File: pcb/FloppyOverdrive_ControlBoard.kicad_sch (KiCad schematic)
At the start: 43 parts, among them J1 174804-1, J2 Motor_Header, J3 Bus_Connector, J4 Sensor_Header, J5 Heads_Header, J6 Step_Header, J7 PIC_ADC_Header, J8 FPGA_IO_Header, J9 HeadOut_Header, SW1 RST_Btn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

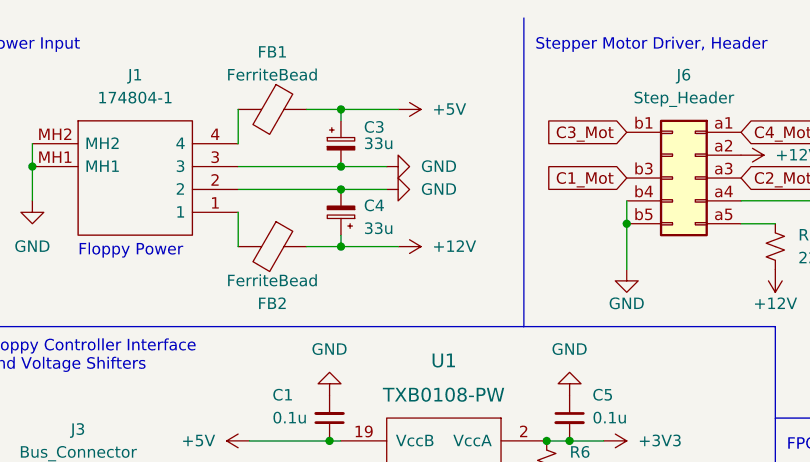
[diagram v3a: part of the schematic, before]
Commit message: Worked on PCB layout, began adding test points
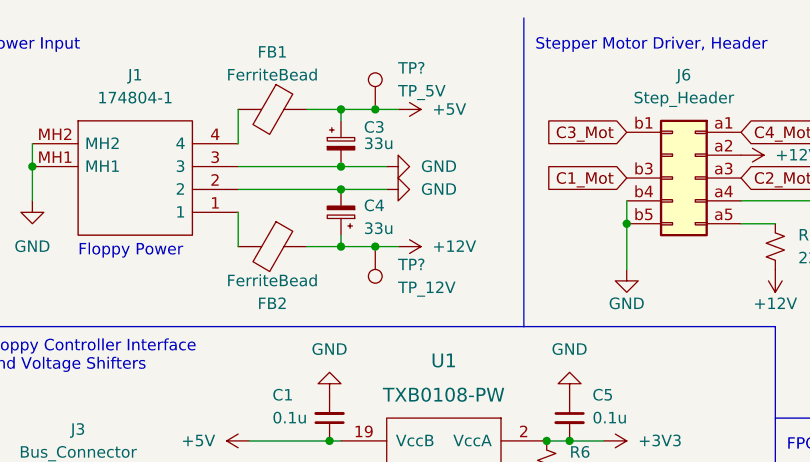
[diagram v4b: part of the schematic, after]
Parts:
- added TP?: TP_5V, symbol Connector:TestPoint
- added TP?: TP_12V, symbol Connector:TestPoint
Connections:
- net +12V: now also TP?.1
- net +5V: now also TP?.1
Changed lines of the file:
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@@
   (junction (at 76.2 185.42) (diameter 0) (color 0 0 0 0)
   )
+  (junction (at 55.88 21.59) (diameter 0) (color 0 0 0 0)
+  )
   (junction (at 77.47 105.41) (diameter 0) (color 0 0 0 0)
   )
@@
   (junction (at 16.51 101.6) (diameter 0) (color 0 0 0 0)
   )
+  (junction (at 55.88 36.83) (diameter 0) (color 0 0 0 0)
+  )
   (junction (at 16.51 83.82) (diameter 0) (color 0 0 0 0)
   )
@@
     (stroke (width 0) (type default) (color 0 0 0 0))
   )
-  (wire (pts (xy 52.07 36.83) (xy 58.42 36.83))
+  (wire (pts (xy 52.07 36.83) (xy 55.88 36.83))
     (stroke (width 0) (type default) (color 0 0 0 0))
   )
@@
     (stroke (width 0) (type default) (color 0 0 0 0))
   )
+  (wire (pts (xy 55.88 21.59) (xy 58.42 21.59))
+    (stroke (width 0) (type default) (color 0 0 0 0))
+  )
   (wire (pts (xy 74.93 71.12) (xy 76.2 71.12))
     (stroke (width 0) (type default) (color 0 0 0 0))
@@
     (stroke (width 0) (type default) (color 0 0 0 0))
   )
+  (wire (pts (xy 55.88 36.83) (xy 58.42 36.83))
+    (stroke (width 0) (type default) (color 0 0 0 0))
+  )
   (wire (pts (xy 24.13 158.75) (xy 26.67 158.75))
     (stroke (width 0) (type default) (color 0 0 0 0))
@@
     (stroke (width 0) (type default) (color 0 0 0 0))
   )
-  (wire (pts (xy 52.07 21.59) (xy 58.42 21.59))
+  (wire (pts (xy 52.07 21.59) (xy 55.88 21.59))
     (stroke (width 0) (type default) (color 0 0 0 0))
   )
@@
     (pin "2")
   )
+  (symbol (lib_id "Connector:TestPoint") (at 55.88 21.59 0) (unit 1)
+    (in_bom yes) (on_board yes) (fields_autoplaced)
+    (property "Reference" "TP?" (id 0) (at 58.42 17.0179 0)
+      (effects (font (size 1.27 1.27)) (justify left))
+    )
+    (property "Value" "TP_5V" (id 1) (at 58.42 19.5579 0)
+      (effects (font (size 1.27 1.27)) (justify left))
+    )
+    (property "Footprint" "" (id 2) (at 60.96 21.59 0)
+      (effects (font (size 1.27 1.27)) hide)
+    )
+    (property "Datasheet" "~" (id 3) (at 60.96 21.59 0)
+      (effects (font (size 1.27 1.27)) hide)
+    )
+    (pin "1")
+  )
   (symbol (lib_id "power:GND") (at 119.38 140.97 270) (unit 1)
     (in_bom yes) (on_board yes) (fields_autoplaced)
@@
     (pin "2")
   )
+  (symbol (lib_id "Connector:TestPoint") (at 55.88 36.83 180) (unit 1)
+    (in_bom yes) (on_board yes) (fields_autoplaced)
+    (property "Reference" "TP?" (id 0) (at 58.42 38.8619 0)
+      (effects (font (size 1.27 1.27)) (justify right))
+    )
+    (property "Value" "TP_12V" (id 1) (at 58.42 41.4019 0)
+      (effects (font (size 1.27 1.27)) (justify right))
+    )
+    (property "Footprint" "" (id 2) (at 50.8 36.83 0)
+      (effects (font (size 1.27 1.27)) hide)
+    )
+    (property "Datasheet" "~" (id 3) (at 50.8 36.83 0)
+      (effects (font (size 1.27 1.27)) hide)
+    )
+    (pin "1")
+  )
   (symbol (lib_id "Connector_Generic:Conn_02x02_Odd_Even") (at 124.46 80.01 0) (unit 1)
     (in_bom yes) (on_board yes) (fields_autoplaced)
@@
       (reference "SW1") (unit 1) (value "RST_Btn") (footprint "Button_Switch_THT:SW_PUSH_6mm")
     )
+    (path "/58a9337f-8e58-4970-873c-354ef45ae12f"
+      (reference "TP?") (unit 1) (value "TP_5V") (footprint "")
+    )
+    (path "/6c7d9ade-e7a5-41ce-947f-92e1c557904b"
+      (reference "TP?") (unit 1) (value "TP_12V") (footprint "")
+    )
     (path "/af8acdcd-2401-4236-bdc2-c260c5079e4e"

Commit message: Routing first draft
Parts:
- added TP3: TP_3V3, TestPoint:TestPoint_Pad_D1.0mm, symbol Connector:TestPoint
- TP1, TP2: renamed from TP?; footprint (none) -> TestPoint:TestPoint_Pad_D1.0mm
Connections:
- net +3.3V: no longer R11.2, U4.J2.34 (3v3)
- net +3V3: now also R11.2, U4.J2.34 (3v3), TP3.1
- net Density: now also U4.J3.20 (F14); no longer U4.J3.1 (A7)
- net DriveSel_0: now also U4.J3.26 (K14); no longer U4.J3.4 (C6)
- net DriveSel_1: now also U4.J3.28 (L14); no longer U4.J3.5 (D6)
- net DriveSel_2: now also U4.J3.30 (L12); no longer U4.J3.6 (D7)
- net DriveSel_3: now also U4.J3.22 (G14); no longer U4.J3.2 (A6)
- net Index: now also U4.J3.24 (H12); no longer U4.J3.3 (C7)
- net Motor: now also U4.J3.32 (P14); no longer U4.J3.7 (A10)
- net Motor_Control: now also U4.J2.29 (M6); no longer U4.J2.7 (C3)
- net PIN_10: now also U4.J3.5 (D6); no longer U4.J3.20 (F14)
- net PIN_12: now also U4.J3.6 (D7); no longer U4.J3.21 (F12)
- net PIN_14: now also U4.J3.7 (A10); no longer U4.J3.22 (G14)
- net PIN_16: now also U4.J3.8 (D10); no longer U4.J3.23 (G12)
- net PIN_18: now also U4.J3.9 (C10); no longer U4.J3.24 (H12)
- net PIN_2: now also U4.J3.1 (A7); no longer U4.J2.31 (M7)
- net PIN_20: now also U4.J3.10 (C11); no longer U4.J3.25 (J12)
- net PIN_22: now also U4.J3.11 (A11); no longer U4.J3.26 (K14)
- net PIN_24: now also U4.J3.12 (A12); no longer U4.J3.27 (H11)
- net PIN_26: now also U4.J3.13 (B14); no longer U4.J3.28 (L14)
- net PIN_28: now also U4.J3.14 (C14); no longer U4.J3.29 (K12)
- net PIN_30: now also U4.J3.15 (C12); no longer U4.J3.30 (L12)
- net PIN_32: now also U4.J3.16 (D14); no longer U4.J3.31 (N14)
- net PIN_34: now also U4.J3.17 (D12); no longer U4.J3.32 (P14)
- net PIN_36: now also U4.J3.18 (E14); no longer U4.J3.33 (M12)
- net PIN_38: now also U4.J2.27 (P3); no longer U4.J3.34 (P8)
- net PIN_4: now also U4.J3.2 (A6); no longer U4.J3.17 (D12)
- net PIN_6: now also U4.J3.3 (C7); no longer U4.J3.18 (E14)
- net PIN_8: now also U4.J3.4 (C6); no longer U4.J3.19 (E12)
- net ReadData: now also U4.J3.23 (G12); no longer U4.J3.14 (C14)
- net Ready: now also U4.J3.19 (E12); no longer U4.J3.16 (D14)
- net SideSel: now also U4.J3.21 (F12); no longer U4.J3.15 (C12)
- net Speed_Control: now also U4.J2.31 (M7); no longer U4.J2.9 (C1)
- net Step: now also U4.J3.33 (M12); no longer U4.J3.9 (C10)
- net StepDir: now also U4.J3.34 (P8); no longer U4.J3.8 (D10)
- net Track0: now also U4.J3.27 (H11); no longer U4.J3.12 (A12)
- net WriteData: now also U4.J3.31 (N14); no longer U4.J3.10 (C11)
- net WriteGate: now also U4.J3.29 (K12); no longer U4.J3.11 (A11)
- net WriteProtect: now also U4.J3.25 (J12); no longer U4.J3.13 (B14)
- net at U4.J2.11 (E1): now also J8.7 (Pin_7); no longer J8.3 (Pin_3)
- net at U4.J2.12 (D1): now also J8.9 (Pin_9); no longer J8.5 (Pin_5)
- net at U4.J2.13 (G1): now also J8.11 (Pin_11); no longer J8.7 (Pin_7)
- net at U4.J2.14 (F3): now also J8.13 (Pin_13); no longer J8.9 (Pin_9)
- net at U4.J2.15 (H1): now also J8.15 (Pin_15); no longer J8.11 (Pin_11)
- net at U4.J2.16 (G3): now also J8.17 (Pin_17); no longer J8.13 (Pin_13)
- net at U4.J2.17 (J1): now also J8.19 (Pin_19); no longer J8.15 (Pin_15)
- net at U4.J2.18 (H3): now also J8.21 (Pin_21); no longer J8.17 (Pin_17)
- net at U4.J2.19 (K3): now also J8.23 (Pin_23); no longer J8.19 (Pin_19)
- net at U4.J2.20 (J3): now also J8.25 (Pin_25); no longer J8.21 (Pin_21)
- net at U4.J2.21 (M1): now also J8.27 (Pin_27); no longer J8.23 (Pin_23)
- net at U4.J2.22 (L1): now also J8.29 (Pin_29); no longer J8.25 (Pin_25)
- net at U4.J2.23 (M3): now also J8.31 (Pin_31); no longer J8.27 (Pin_27)
- net at U4.J2.24 (N1): now also J8.33 (Pin_33); no longer J8.29 (Pin_29)
- net at U4.J2.25 (P2): now also J8.35 (Pin_35); no longer J8.31 (Pin_31)
- net at U4.J2.26 (P1): now also J8.37 (Pin_37); no longer J8.33 (Pin_33)
- new net: J8.3 (Pin_3), U4.J2.7 (C3)
- new net: J8.5 (Pin_5), U4.J2.9 (C1)
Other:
- moved on the sheet: J7, J8, R11, SW1

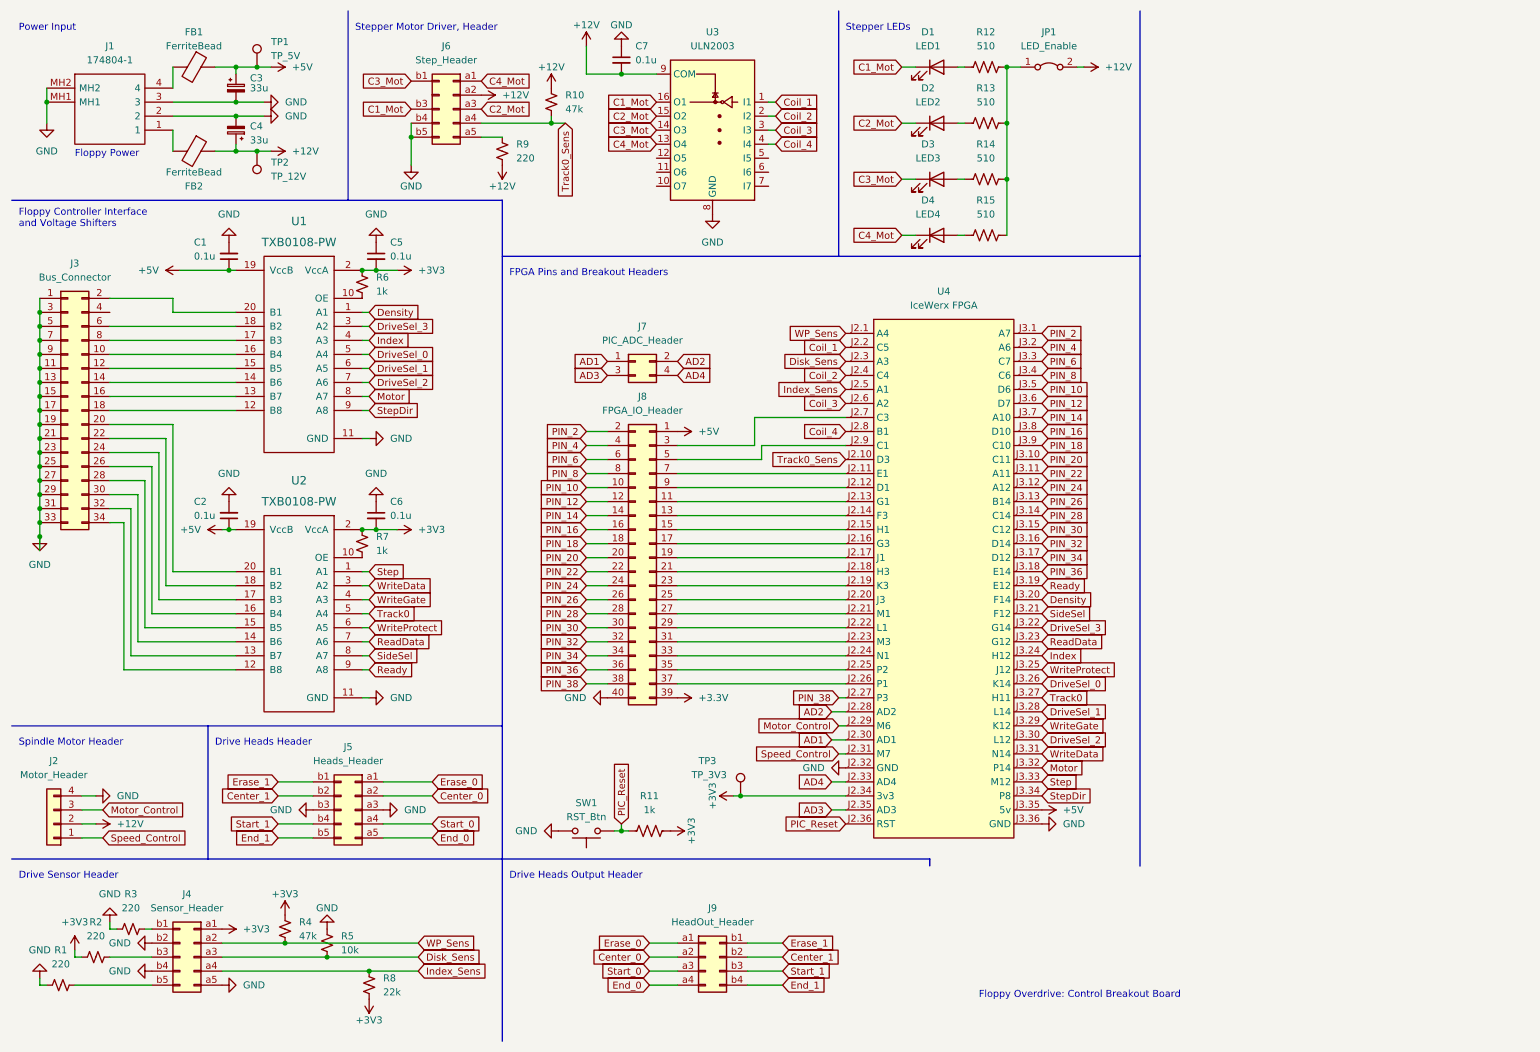
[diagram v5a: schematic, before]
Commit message: Fixed floppy bus orientation
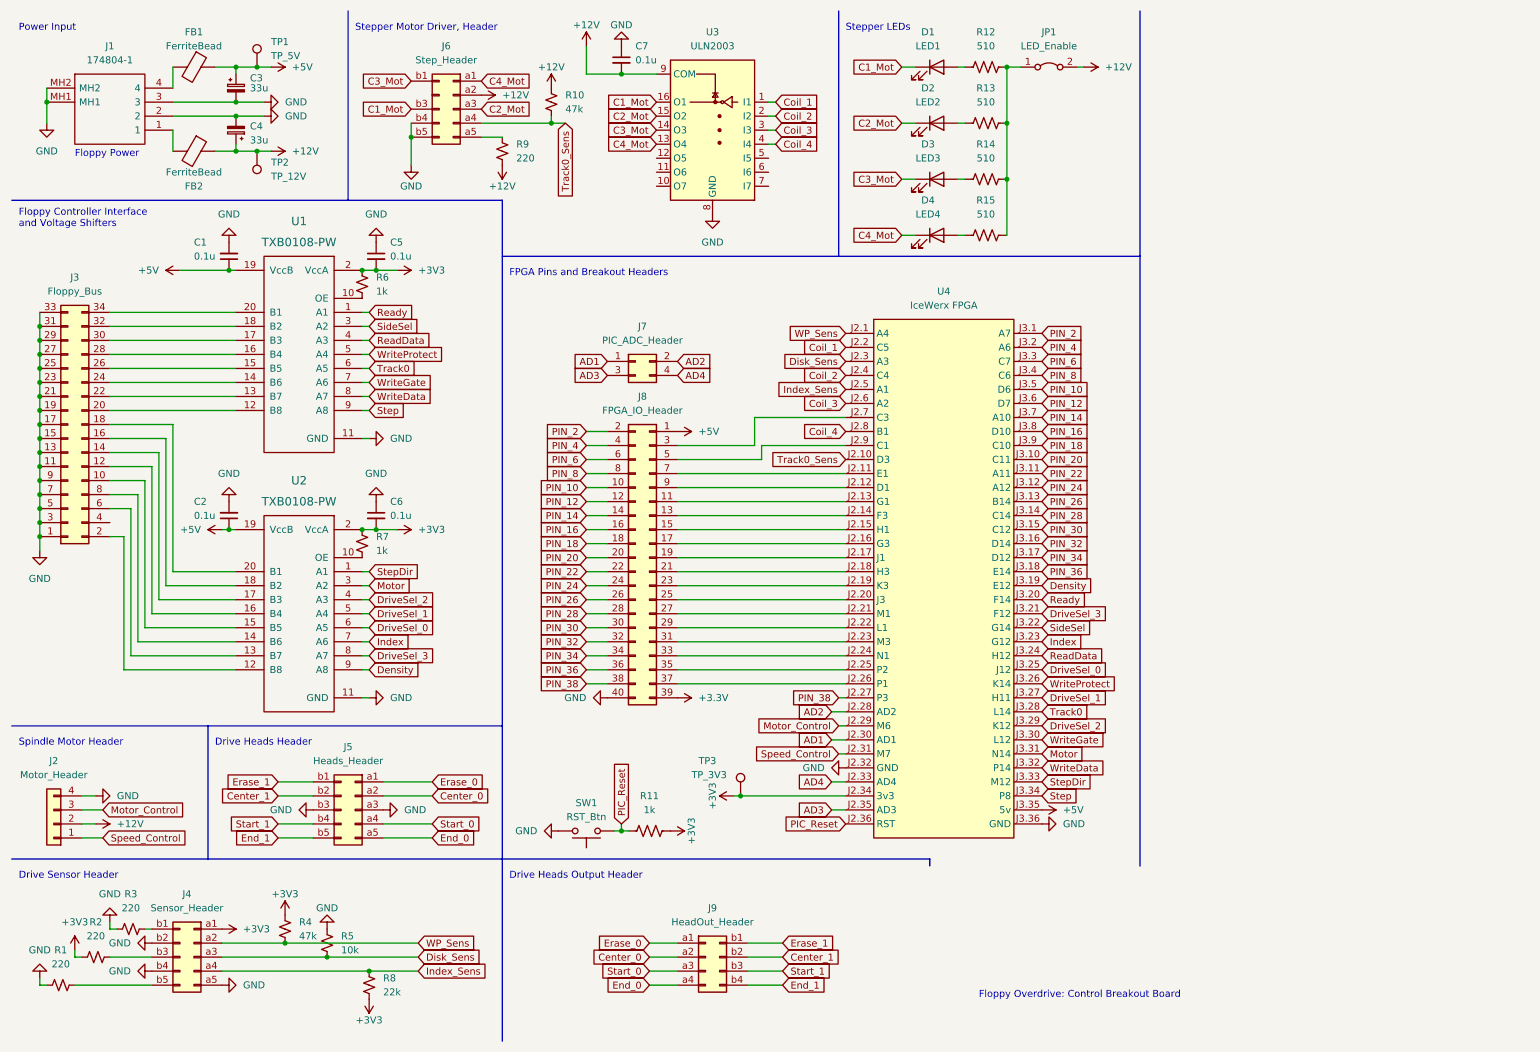
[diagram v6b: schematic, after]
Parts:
- J3: value Bus_Connector -> Floppy_Bus; footprint Connector_PinHeader_2.54mm:PinHeader_2x17_P2.54mm_Horizontal -> Connector_PinHeader_2.54mm:PinHeader_2x17_P2.54mm_Vertical
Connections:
- net Density: now also U2.9 (A8), U4.J3.19 (E12); no longer U1.1 (A1), U4.J3.20 (F14)
- net DriveSel_0: now also U2.6 (A5), U4.J3.25 (J12); no longer U1.5 (A4), U4.J3.26 (K14)
- net DriveSel_1: now also U2.5 (A4), U4.J3.27 (H11); no longer U1.6 (A5), U4.J3.28 (L14)
- net DriveSel_2: now also U2.4 (A3), U4.J3.29 (K12); no longer U1.7 (A6), U4.J3.30 (L12)
- net DriveSel_3: now also U2.8 (A7), U4.J3.21 (F12); no longer U1.3 (A2), U4.J3.22 (G14)
- net Index: now also U2.7 (A6), U4.J3.23 (G12); no longer U1.4 (A3), U4.J3.24 (H12)
- net Motor: now also U2.3 (A2), U4.J3.31 (N14); no longer U1.8 (A7), U4.J3.32 (P14)
- net ReadData: now also U1.4 (A3), U4.J3.24 (H12); no longer U2.7 (A6), U4.J3.23 (G12)
- net Ready: now also U1.1 (A1), U4.J3.20 (F14); no longer U2.9 (A8), U4.J3.19 (E12)
- net SideSel: now also U1.3 (A2), U4.J3.22 (G14); no longer U2.8 (A7), U4.J3.21 (F12)
- net Step: now also U1.9 (A8), U4.J3.34 (P8); no longer U2.1 (A1), U4.J3.33 (M12)
- net StepDir: now also U2.1 (A1), U4.J3.33 (M12); no longer U1.9 (A8), U4.J3.34 (P8)
- net Track0: now also U1.6 (A5), U4.J3.28 (L14); no longer U2.5 (A4), U4.J3.27 (H11)
- net WriteData: now also U1.8 (A7), U4.J3.32 (P14); no longer U2.3 (A2), U4.J3.31 (N14)
- net WriteGate: now also U1.7 (A6), U4.J3.30 (L12); no longer U2.4 (A3), U4.J3.29 (K12)
- net WriteProtect: now also U1.5 (A4), U4.J3.26 (K14); no longer U2.6 (A5), U4.J3.25 (J12)
- net at U2.12 (B8): now also J3.2 (Pin_2); no longer J3.34 (Pin_34)
- net at U2.13 (B7): now also J3.6 (Pin_6); no longer J3.32 (Pin_32)
- net at U2.14 (B6): now also J3.8 (Pin_8); no longer J3.30 (Pin_30)
- net at U2.15 (B5): now also J3.10 (Pin_10); no longer J3.28 (Pin_28)
- net at U2.16 (B4): now also J3.12 (Pin_12); no longer J3.26 (Pin_26)
- net at U2.17 (B3): now also J3.14 (Pin_14); no longer J3.24 (Pin_24)
- net at U2.18 (B2): now also J3.16 (Pin_16); no longer J3.22 (Pin_22)
- net at U2.20 (B1): now also J3.18 (Pin_18); no longer J3.20 (Pin_20)
- net at U1.16 (B4): now also J3.28 (Pin_28); no longer J3.10 (Pin_10)
- net at U1.15 (B5): now also J3.26 (Pin_26); no longer J3.12 (Pin_12)
- net at U1.14 (B6): now also J3.24 (Pin_24); no longer J3.14 (Pin_14)
- net at U1.13 (B7): now also J3.22 (Pin_22); no longer J3.16 (Pin_16)
- net at U1.12 (B8): now also J3.20 (Pin_20); no longer J3.18 (Pin_18)
- net at U1.20 (B1): now also J3.34 (Pin_34); no longer J3.2 (Pin_2)
- net at U1.18 (B2): now also J3.32 (Pin_32); no longer J3.6 (Pin_6)
- net at U1.17 (B3): now also J3.30 (Pin_30); no longer J3.8 (Pin_8)
